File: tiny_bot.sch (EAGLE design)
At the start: 33 parts, among them IC1 SN754410PDIP, U1 ATMEGA328P_PDIP, X1 16 MHz

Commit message: Finished schematic and added board file
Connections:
- removed net N$15: IC1.1Y
- removed net N$18: IC1.2Y
- removed net N$25: IC1.4Y
- removed net N$28: IC1.3Y
- new net LEFT_PIN_1: IC1.1Y, LEFT_MOTOR.1
- new net LEFT_PIN_2: IC1.2Y, LEFT_MOTOR.2
- new net RIGHT_PIN_1: IC1.3Y, RIGHT_MOTOR.1
- new net RIGHT_PIN_2: IC1.4Y, RIGHT_MOTOR.2
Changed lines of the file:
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@@
-</segment>
-</net>
-<net name="N$15" class="0">
-<segment>
-<pinref part="IC1" gate="G$1" pin="1Y"/>
-<wire x1="195.58" y1="78.74" x2="187.96" y2="78.74" width="0.1524" layer="91"/>
-</segment>
-</net>
-<net name="N$18" class="0">
-<segment>
-<pinref part="IC1" gate="G$1" pin="2Y"/>
-<wire x1="195.58" y1="71.12" x2="187.96" y2="71.12" width="0.1524" layer="91"/>
-</segment>
-</net>
-<net name="N$25" class="0">
-<segment>
-<pinref part="IC1" gate="G$1" pin="4Y"/>
-<wire x1="220.98" y1="78.74" x2="228.6" y2="78.74" width="0.1524" layer="91"/>
-</segment>
-</net>
-<net name="N$28" class="0">
-<segment>
-<pinref part="IC1" gate="G$1" pin="3Y"/>
-<wire x1="220.98" y1="71.12" x2="228.6" y2="71.12" width="0.1524" layer="91"/>
 </segment>
 </net>
@@
 </segment>
 </net>
+<net name="LEFT_PIN_1" class="0">
+<segment>
+<pinref part="LEFT_MOTOR" gate="G$1" pin="1"/>
+<wire x1="271.78" y1="93.98" x2="266.7" y2="93.98" width="0.1524" layer="91"/>
+<label x="257.81" y="93.98" size="1.778" layer="95"/>
+</segment>
+<segment>
+<pinref part="IC1" gate="G$1" pin="1Y"/>
+<wire x1="195.58" y1="78.74" x2="187.96" y2="78.74" width="0.1524" layer="91"/>
+<label x="181.61" y="78.74" size="1.778" layer="95"/>
+</segment>
+</net>
+<net name="LEFT_PIN_2" class="0">
+<segment>
+<pinref part="LEFT_MOTOR" gate="G$1" pin="2"/>
+<wire x1="271.78" y1="91.44" x2="266.7" y2="91.44" width="0.1524" layer="91"/>
+<label x="257.81" y="91.44" size="1.778" layer="95"/>
+</segment>
+<segment>
+<pinref part="IC1" gate="G$1" pin="2Y"/>
+<wire x1="195.58" y1="71.12" x2="187.96" y2="71.12" width="0.1524" layer="91"/>
+<label x="181.61" y="71.12" size="1.778" layer="95"/>
+</segment>
+</net>
+<net name="RIGHT_PIN_1" class="0">
+<segment>
+<pinref part="RIGHT_MOTOR" gate="G$1" pin="1"/>
+<wire x1="271.78" y1="78.74" x2="266.7" y2="78.74" width="0.1524" layer="91"/>
+<label x="256.54" y="78.74" size="1.778" layer="95"/>
+</segment>
+<segment>
+<pinref part="IC1" gate="G$1" pin="3Y"/>
+<wire x1="220.98" y1="71.12" x2="228.6" y2="71.12" width="0.1524" layer="91"/>
+<label x="220.98" y="71.12" size="1.778" layer="95"/>
+</segment>
+</net>
+<net name="RIGHT_PIN_2" class="0">
+<segment>
+<pinref part="RIGHT_MOTOR" gate="G$1" pin="2"/>
+<wire x1="271.78" y1="76.2" x2="266.7" y2="76.2" width="0.1524" layer="91"/>
+<label x="256.54" y="76.2" size="1.778" layer="95"/>
+</segment>
+<segment>
+<pinref part="IC1" gate="G$1" pin="4Y"/>
+<wire x1="220.98" y1="78.74" x2="228.6" y2="78.74" width="0.1524" layer="91"/>
+<label x="220.98" y="78.74" size="1.778" layer="95"/>
+</segment>
+</net>

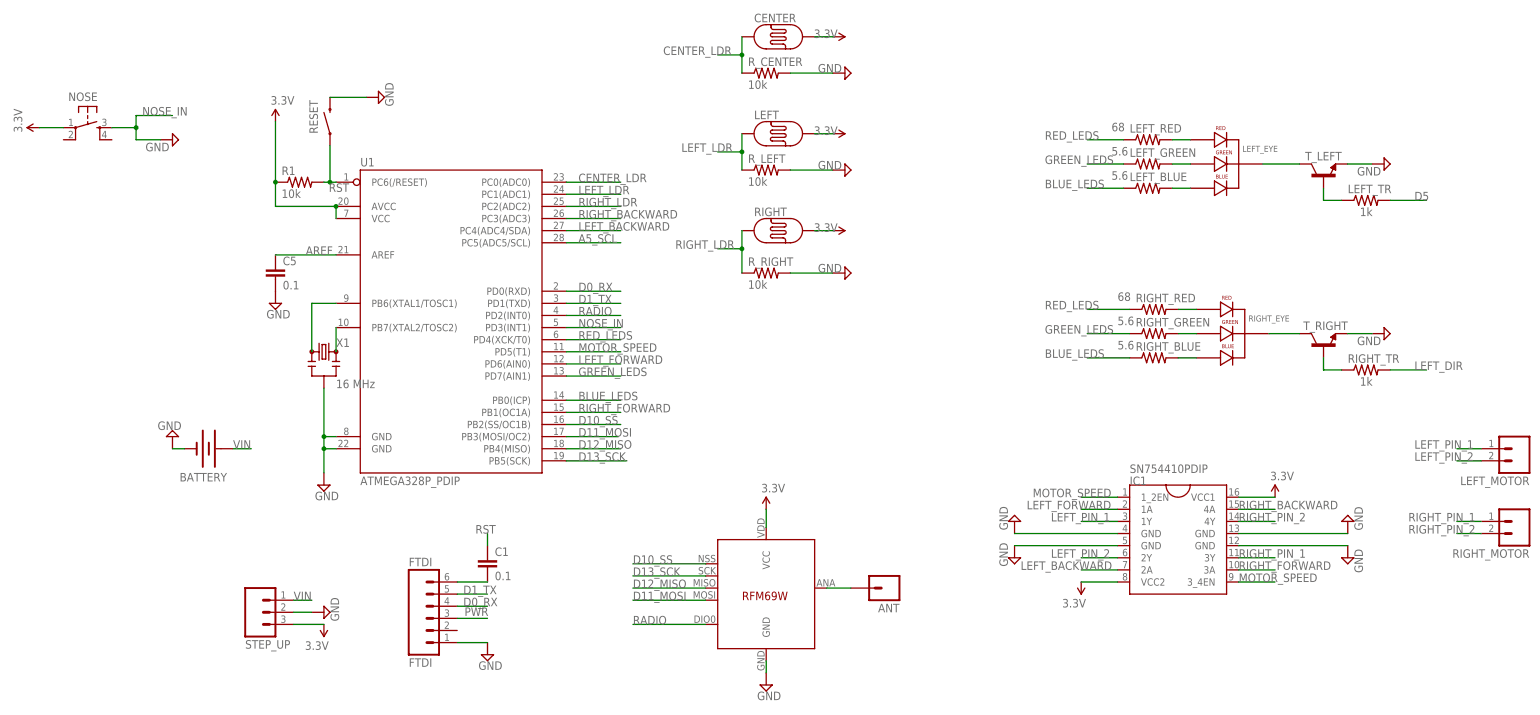
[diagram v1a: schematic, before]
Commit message: Fixed LED problem; Started board layout
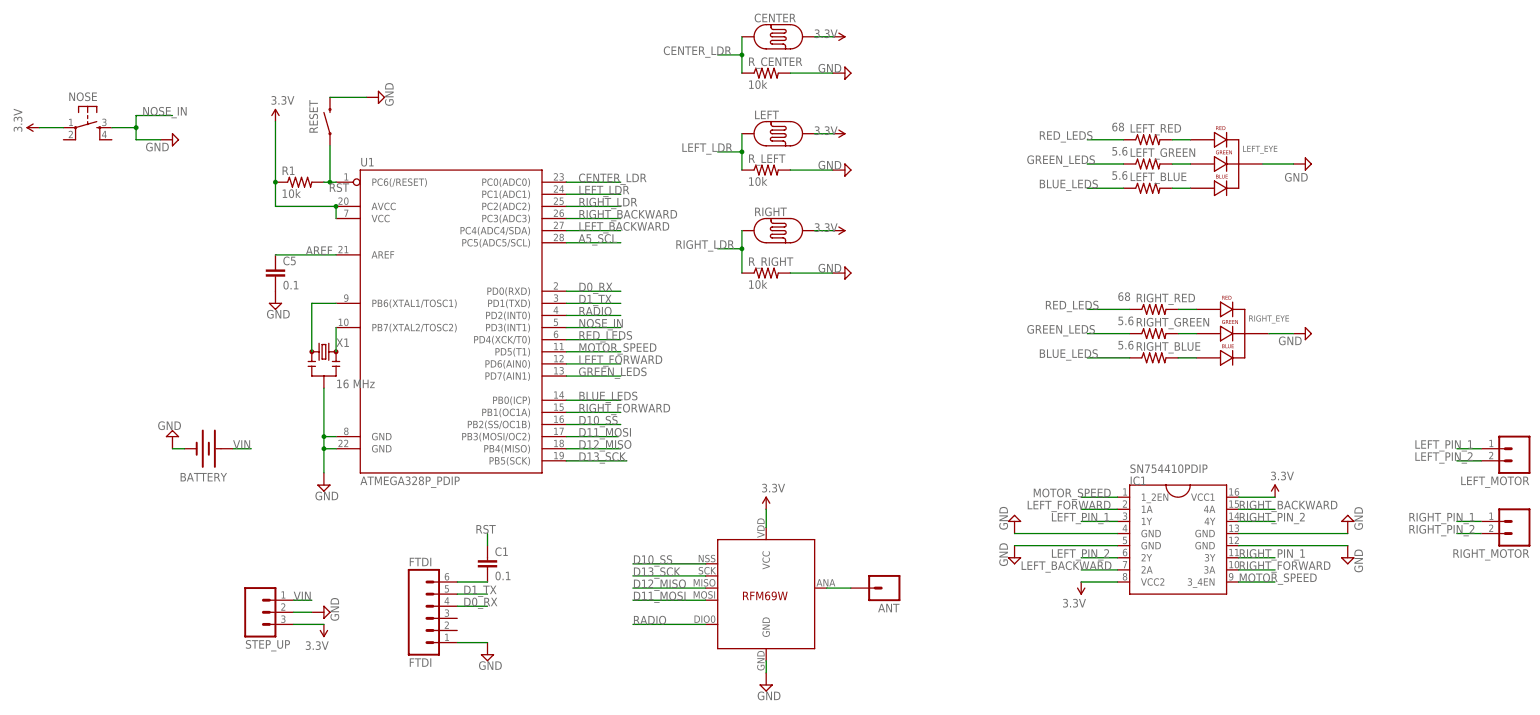
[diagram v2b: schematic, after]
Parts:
- removed LEFT_TR, RIGHT_TR: 1k, SparkFun-Passives:RESISTORPTH-1/4W
- removed T_LEFT, T_RIGHT: (no value), SparkFun-DiscreteSemi:TRANSISTOR_NPNP2N2222A
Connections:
- removed net D5: LEFT_TR.2
- removed net LEFT_DIR: RIGHT_TR.2
- removed net N$10: RIGHT_EYE.CATHODE, T_RIGHT.C
- removed net N$11: LEFT_TR.1, T_LEFT.B
- removed net N$12: RIGHT_TR.1, T_RIGHT.B
- removed net N$9: LEFT_EYE.CATHODE, T_LEFT.C
- removed net PWR: FTDI.3
- net GND: now also LEFT_EYE.CATHODE, RIGHT_EYE.CATHODE; no longer T_LEFT.E, T_RIGHT.E
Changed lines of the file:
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@@
 <part name="RIGHT_GREEN" library="SparkFun-Passives" deviceset="RESISTOR" device="PTH-1/4W" value="5.6"/>
 <part name="RIGHT_BLUE" library="SparkFun-Passives" deviceset="RESISTOR" device="PTH-1/4W" value="5.6"/>
-<part name="T_LEFT" library="SparkFun-DiscreteSemi" deviceset="TRANSISTOR_NPN" device="P2N2222A"/>
-<part name="T_RIGHT" library="SparkFun-DiscreteSemi" deviceset="TRANSISTOR_NPN" device="P2N2222A"/>
-<part name="RIGHT_TR" library="SparkFun-Passives" deviceset="RESISTOR" device="PTH-1/4W" value="1k"/>
-<part name="LEFT_TR" library="SparkFun-Passives" deviceset="RESISTOR" device="PTH-1/4W" value="1k"/>
 <part name="IC1" library="AlexW-Eagle-Libraries" deviceset="SN754410" device="PDIP"/>
 <part name="SUPPLY20" library="supply2" deviceset="GND" device=""/>
@@
 <attribute name="VALUE" x="137.795" y="132.715" size="1.778" layer="96" rot="R180"/>
 </instance>
-<instance part="SUPPLY18" gate="GND" x="251.46" y="153.67" smashed="yes" rot="R90">
-<attribute name="VALUE" x="250.825" y="153.035" size="1.778" layer="96" rot="R180"/>
-</instance>
-<instance part="SUPPLY19" gate="GND" x="251.46" y="118.11" smashed="yes" rot="R90">
-<attribute name="VALUE" x="250.825" y="117.475" size="1.778" layer="96" rot="R180"/>
+<instance part="SUPPLY18" gate="GND" x="234.95" y="153.67" smashed="yes" rot="R90">
+<attribute name="VALUE" x="235.585" y="151.765" size="1.778" layer="96" rot="R180"/>
+</instance>
+<instance part="SUPPLY19" gate="GND" x="234.95" y="118.11" smashed="yes" rot="R90">
+<attribute name="VALUE" x="234.315" y="117.475" size="1.778" layer="96" rot="R180"/>
 </instance>
 <instance part="LEFT_RED" gate="G$1" x="201.93" y="158.75" smashed="yes">
@@
 <attribute name="NAME" x="199.39" y="114.5286" size="1.778" layer="95"/>
 <attribute name="VALUE" x="195.58" y="114.808" size="1.778" layer="96"/>
-</instance>
-<instance part="T_LEFT" gate="G$1" x="238.76" y="151.13" smashed="yes" rot="R90">
-<attribute name="NAME" x="242.57" y="156.21" size="1.778" layer="95" rot="R180"/>
-<attribute name="VALUE" x="241.3" y="156.21" size="1.778" layer="96" rot="R90"/>
-</instance>
-<instance part="T_RIGHT" gate="G$1" x="238.76" y="115.57" smashed="yes" rot="R90">
-<attribute name="NAME" x="243.84" y="120.65" size="1.778" layer="95" rot="R180"/>
-<attribute name="VALUE" x="241.3" y="120.65" size="1.778" layer="96" rot="R90"/>
-</instance>
-<instance part="RIGHT_TR" gate="G$1" x="247.65" y="110.49" smashed="yes">
-<attribute name="NAME" x="243.84" y="111.9886" size="1.778" layer="95"/>
-<attribute name="VALUE" x="246.38" y="107.188" size="1.778" layer="96"/>
-</instance>
-<instance part="LEFT_TR" gate="G$1" x="247.65" y="146.05" smashed="yes">
-<attribute name="NAME" x="243.84" y="147.5486" size="1.778" layer="95"/>
-<attribute name="VALUE" x="246.38" y="142.748" size="1.778" layer="96"/>
 </instance>
 <instance part="IC1" gate="G$1" x="208.28" y="76.2"/>
@@
 </segment>
 <segment>
-<pinref part="T_LEFT" gate="G$1" pin="E"/>
 <pinref part="SUPPLY18" gate="GND" pin="GND"/>
-<wire x1="243.84" y1="153.67" x2="248.92" y2="153.67" width="0.1524" layer="91"/>
+<pinref part="LEFT_EYE" gate="G$1" pin="CATHODE"/>
+<wire x1="226.06" y1="153.67" x2="232.41" y2="153.67" width="0.1524" layer="91"/>
 </segment>
 <segment>
 <pinref part="SUPPLY19" gate="GND" pin="GND"/>
-<pinref part="T_RIGHT" gate="G$1" pin="E"/>
-<wire x1="248.92" y1="118.11" x2="243.84" y2="118.11" width="0.1524" layer="91"/>
+<pinref part="RIGHT_EYE" gate="G$1" pin="CATHODE"/>
+<wire x1="227.33" y1="118.11" x2="232.41" y2="118.11" width="0.1524" layer="91"/>
 </segment>
 <segment>
@@
 <pinref part="C5" gate="G$1" pin="1"/>
 <pinref part="U1" gate="G$1" pin="AREF"/>
-</segment>
-</net>
-<net name="PWR" class="1">
-<segment>
-<wire x1="57.15" y1="58.42" x2="63.5" y2="58.42" width="0.1524" layer="91"/>
-<label x="58.674" y="58.928" size="1.778" layer="95"/>
-<pinref part="FTDI" gate="G$1" pin="3"/>
 </segment>
 </net>
@@
 <pinref part="LEFT_BLUE" gate="G$1" pin="1"/>
 <wire x1="196.85" y1="148.59" x2="189.23" y2="148.59" width="0.1524" layer="91"/>
-<label x="180.34" y="148.59" size="1.778" layer="95"/>
+<label x="179.07" y="148.59" size="1.778" layer="95"/>
 </segment>
 <segment>
 <pinref part="RIGHT_BLUE" gate="G$1" pin="1"/>
 <wire x1="198.12" y1="113.03" x2="189.23" y2="113.03" width="0.1524" layer="91"/>
-<label x="180.34" y="113.03" size="1.778" layer="95"/>
+<label x="179.07" y="113.03" size="1.778" layer="95"/>
 </segment>
 </net>
@@
 <pinref part="LEFT_GREEN" gate="G$1" pin="1"/>
 <wire x1="196.85" y1="153.67" x2="189.23" y2="153.67" width="0.1524" layer="91"/>
-<label x="180.34" y="153.67" size="1.778" layer="95"/>
+<label x="176.53" y="153.67" size="1.778" layer="95"/>
 </segment>
 <segment>
 <pinref part="RIGHT_GREEN" gate="G$1" pin="1"/>
 <wire x1="198.12" y1="118.11" x2="189.23" y2="118.11" width="0.1524" layer="91"/>
-<label x="180.34" y="118.11" size="1.778" layer="95"/>
-</segment>
-</net>
-<net name="LEFT_DIR" class="0">
-<segment>
-<pinref part="RIGHT_TR" gate="G$1" pin="2"/>
-<wire x1="252.73" y1="110.49" x2="260.35" y2="110.49" width="0.1524" layer="91"/>
-<label x="257.81" y="110.49" size="1.778" layer="95"/>
-</segment>
-</net>
-<net name="D5" class="0">
-<segment>
-<pinref part="LEFT_TR" gate="G$1" pin="2"/>
-<wire x1="252.73" y1="146.05" x2="260.35" y2="146.05" width="0.1524" layer="91"/>
-<label x="257.81" y="146.05" size="1.778" layer="95"/>
+<label x="176.53" y="118.11" size="1.778" layer="95"/>
 </segment>
 </net>
@@
 <pinref part="LEFT_RED" gate="G$1" pin="1"/>
 <wire x1="196.85" y1="158.75" x2="189.23" y2="158.75" width="0.1524" layer="91"/>
-<label x="180.34" y="158.75" size="1.778" layer="95"/>
+<label x="179.07" y="158.75" size="1.778" layer="95"/>
 </segment>
 <segment>
@@
 </segment>
 </net>
-<net name="N$9" class="0">
-<segment>
-<pinref part="T_LEFT" gate="G$1" pin="C"/>
-<wire x1="226.06" y1="153.67" x2="233.68" y2="153.67" width="0.1524" layer="91"/>
-<pinref part="LEFT_EYE" gate="G$1" pin="CATHODE"/>
-</segment>
-</net>
-<net name="N$10" class="0">
-<segment>
-<pinref part="T_RIGHT" gate="G$1" pin="C"/>
-<pinref part="RIGHT_EYE" gate="G$1" pin="CATHODE"/>
-<wire x1="233.68" y1="118.11" x2="227.33" y2="118.11" width="0.1524" layer="91"/>
-</segment>
-</net>
-<net name="N$11" class="0">
-<segment>
-<pinref part="T_LEFT" gate="G$1" pin="B"/>
-<wire x1="238.76" y1="148.59" x2="238.76" y2="146.05" width="0.1524" layer="91"/>
-<pinref part="LEFT_TR" gate="G$1" pin="1"/>
-<wire x1="238.76" y1="146.05" x2="242.57" y2="146.05" width="0.1524" layer="91"/>
-</segment>
-</net>
-<net name="N$12" class="0">
-<segment>
-<pinref part="T_RIGHT" gate="G$1" pin="B"/>
-<wire x1="238.76" y1="113.03" x2="238.76" y2="110.49" width="0.1524" layer="91"/>
-<wire x1="238.76" y1="110.49" x2="242.57" y2="110.49" width="0.1524" layer="91"/>
-<pinref part="RIGHT_TR" gate="G$1" pin="1"/>
-</segment>
-</net>
